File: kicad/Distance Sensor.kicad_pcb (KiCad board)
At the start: 2 copper layers, 32.5 x 24 mm, 5 parts, among them J1 Conn_01x03, U1 ESP32 C3 Super Mini, U2 VL53LDK

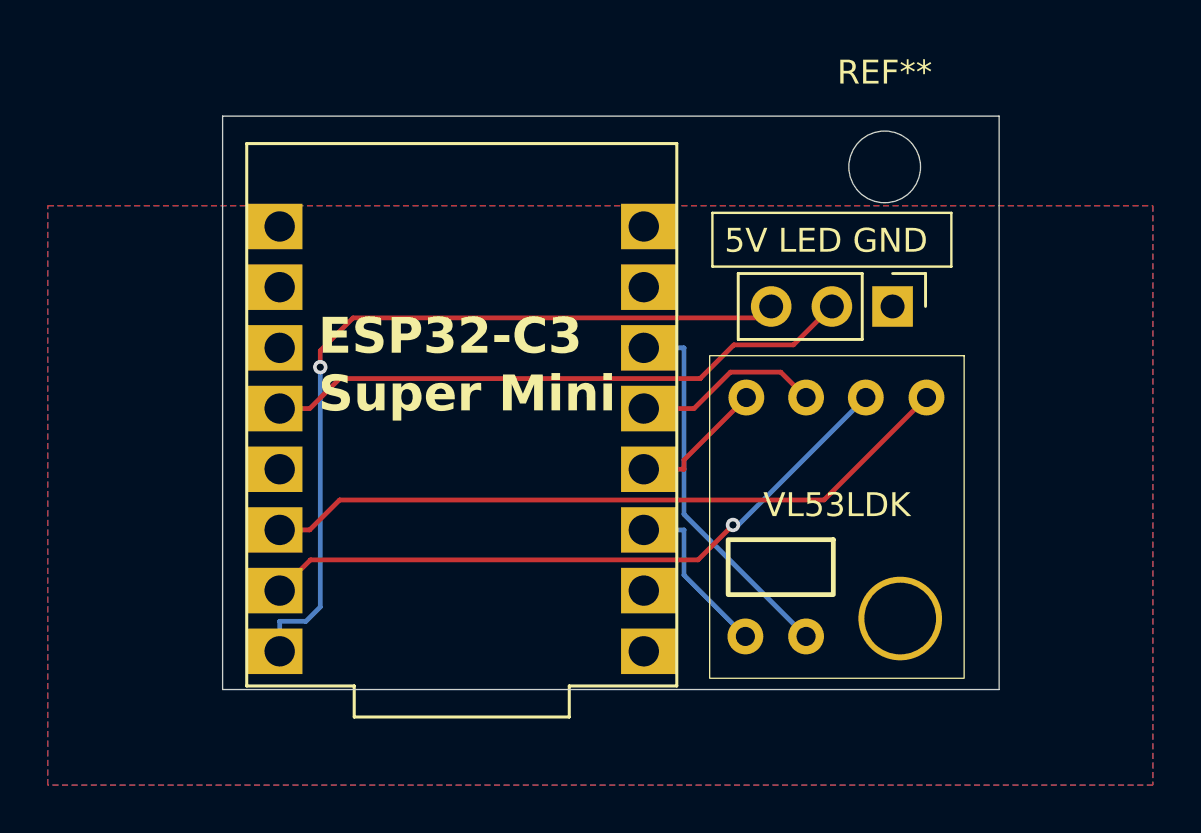
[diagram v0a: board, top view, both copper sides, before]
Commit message: Improve footprints
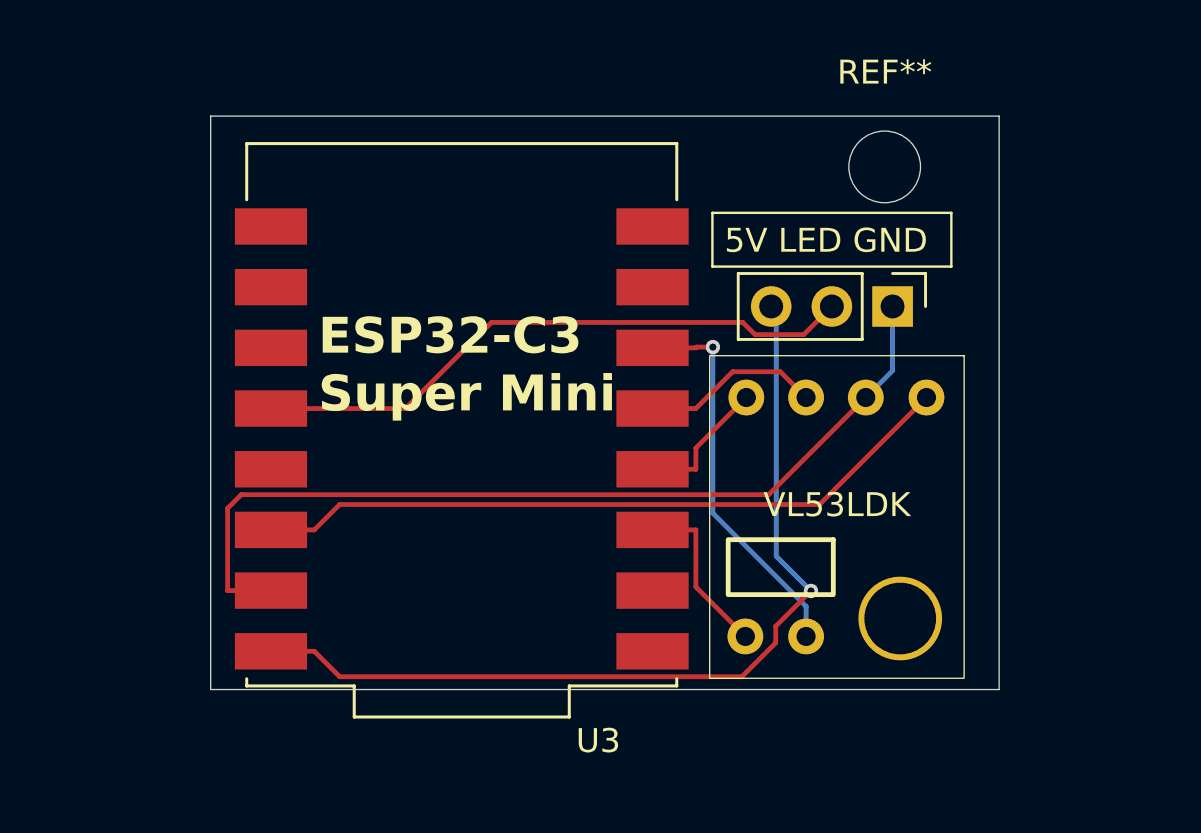
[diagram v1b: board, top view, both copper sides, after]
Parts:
- removed U1: ESP32 C3 Super Mini, Distance Sensor:ESP32-C3 Super Mini
- added U3: ESP32-C3_SUPERMINI_SMD, Distance Sensor:MODULE_ESP32-C3_SUPERMINI, F.Cu at (138.5, 66.0)
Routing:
- net GND: track 28.1 -> 38.2 mm, vias 1 -> 0
- net +5V: track 33.6 -> 37.5 mm
- net Net-(J1-Pin_2): track 24.9 -> 25.7 mm
- net Net-(U2-XSHUT): track 15.9 -> 16.3 mm, vias 0 -> 1
- removed copper zone on B.Cu, net GND
- removed copper zone on F.Cu, net GND
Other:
- board size 32.5 x 24 mm -> 33 x 24 mm
